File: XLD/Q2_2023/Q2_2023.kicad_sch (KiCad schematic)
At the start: 0 parts

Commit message: more updates
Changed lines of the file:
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@@
 (kicad_sch (version 20230121) (generator eeschema)
   (paper "A4")
-  (wire (pts (xy 263.525 36.195) (xy 263.525 37.465))
-    (stroke (width 0) (type default))
-  )
   (text "iqm5q\n" (at 91.44 36.195 0)
     (effects (font (size 5 5)) (justify left bottom))

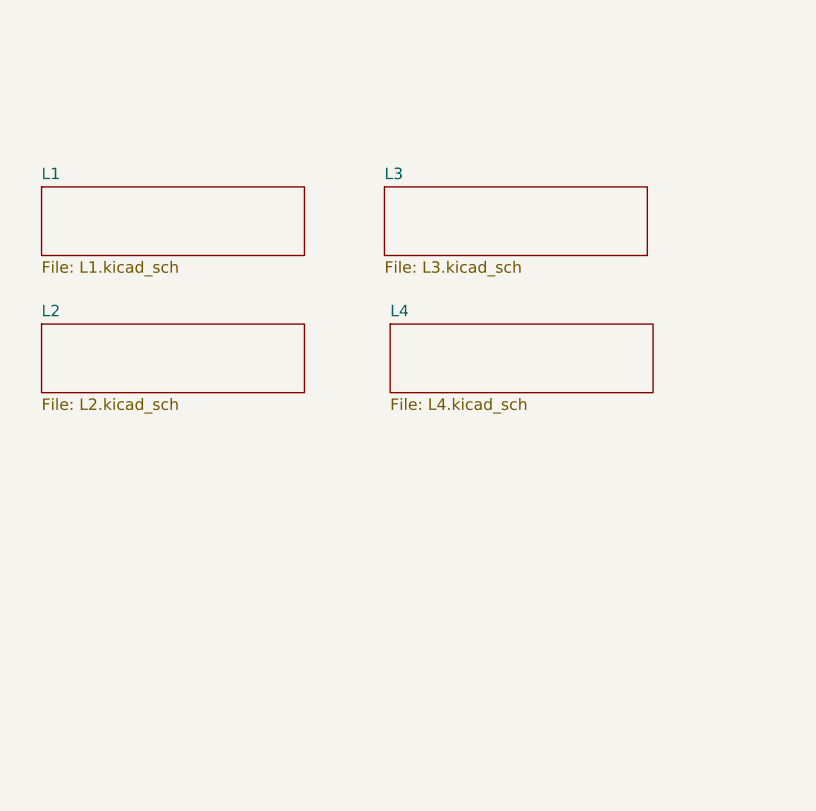
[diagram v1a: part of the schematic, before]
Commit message: update attenuators and pumplines
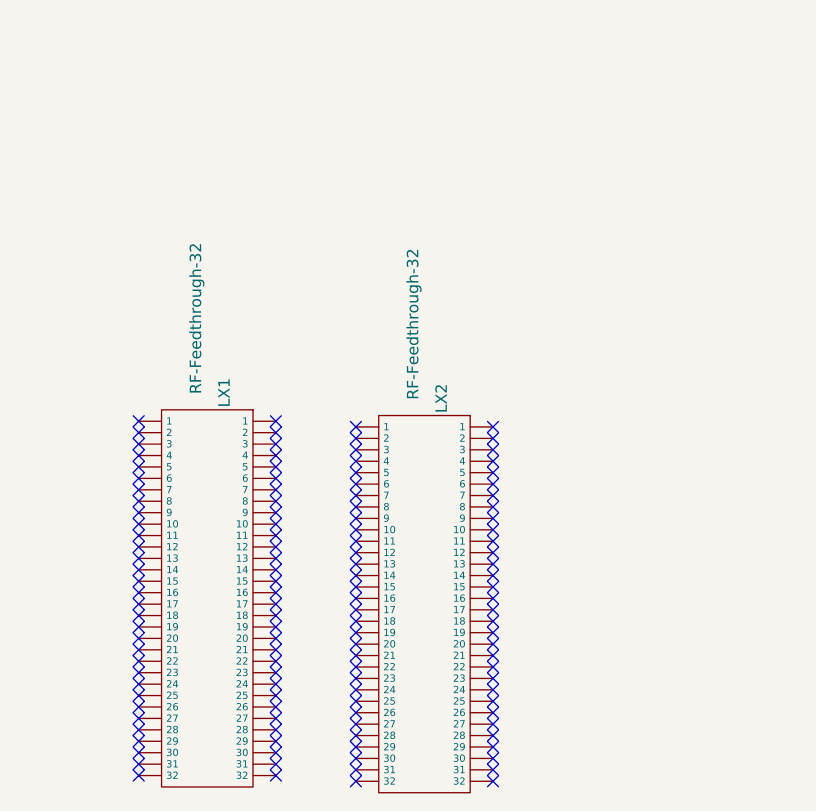
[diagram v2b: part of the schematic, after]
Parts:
- added LX1, LX2: RF-Feedthrough-32, symbol Quantum Computing:RF-Feedthrough-32
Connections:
- no-connect marks 0 -> 128
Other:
- removed sheet L1
- removed sheet L2
- removed sheet L3
- removed sheet L4

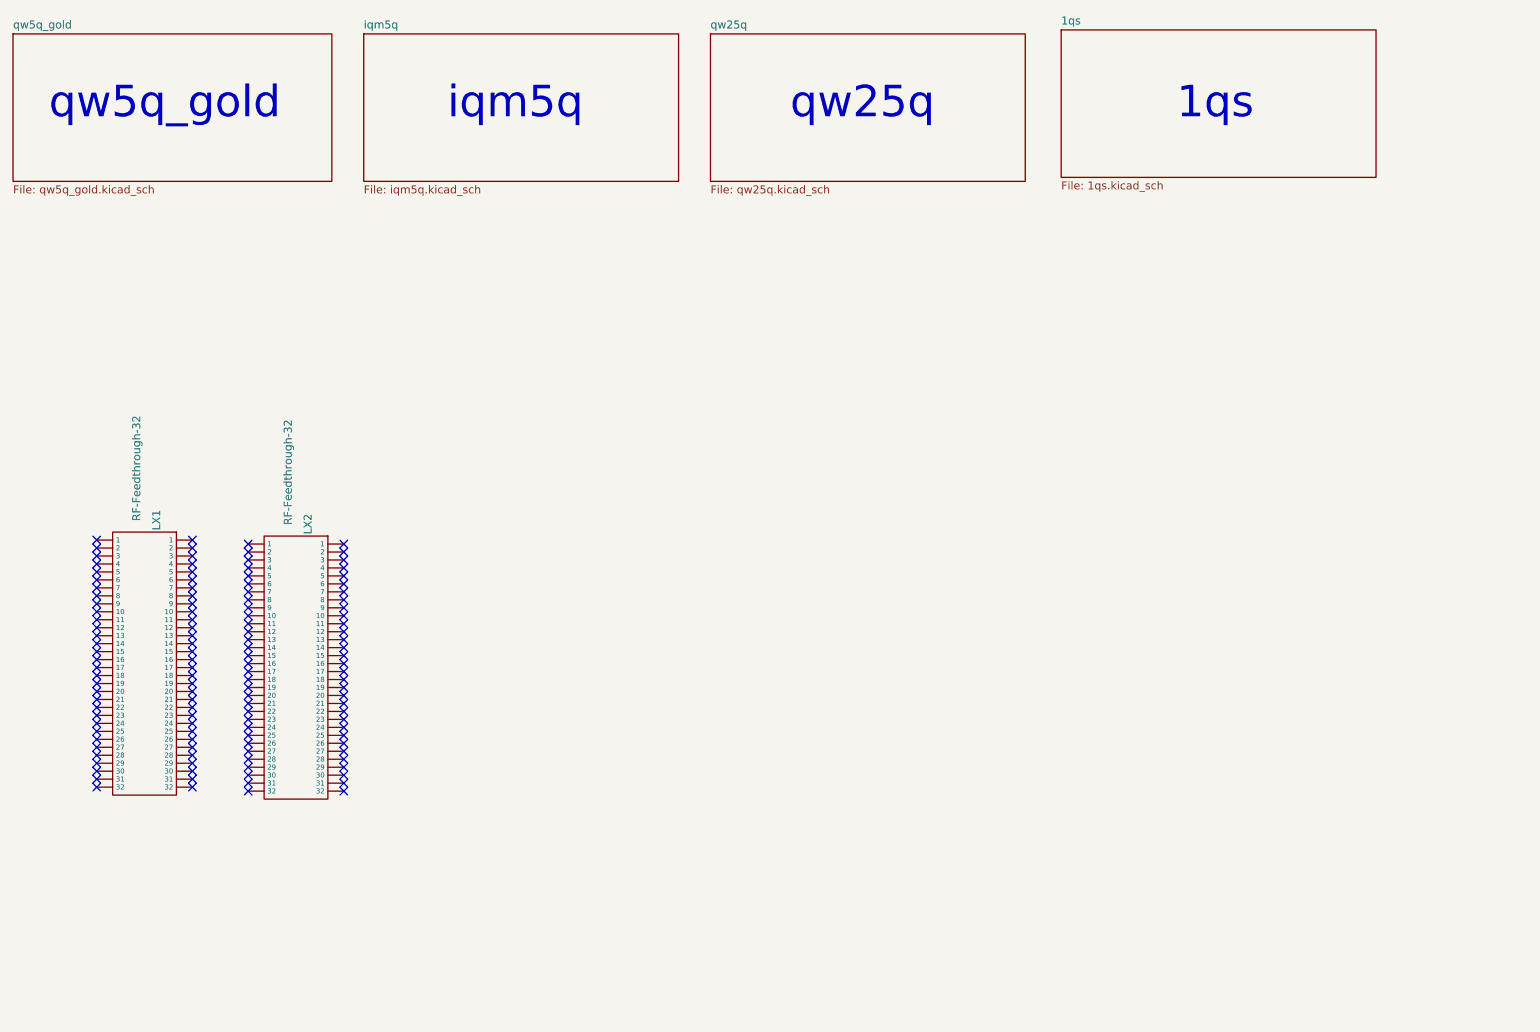
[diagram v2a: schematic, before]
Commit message: Improvements to library components, title, date
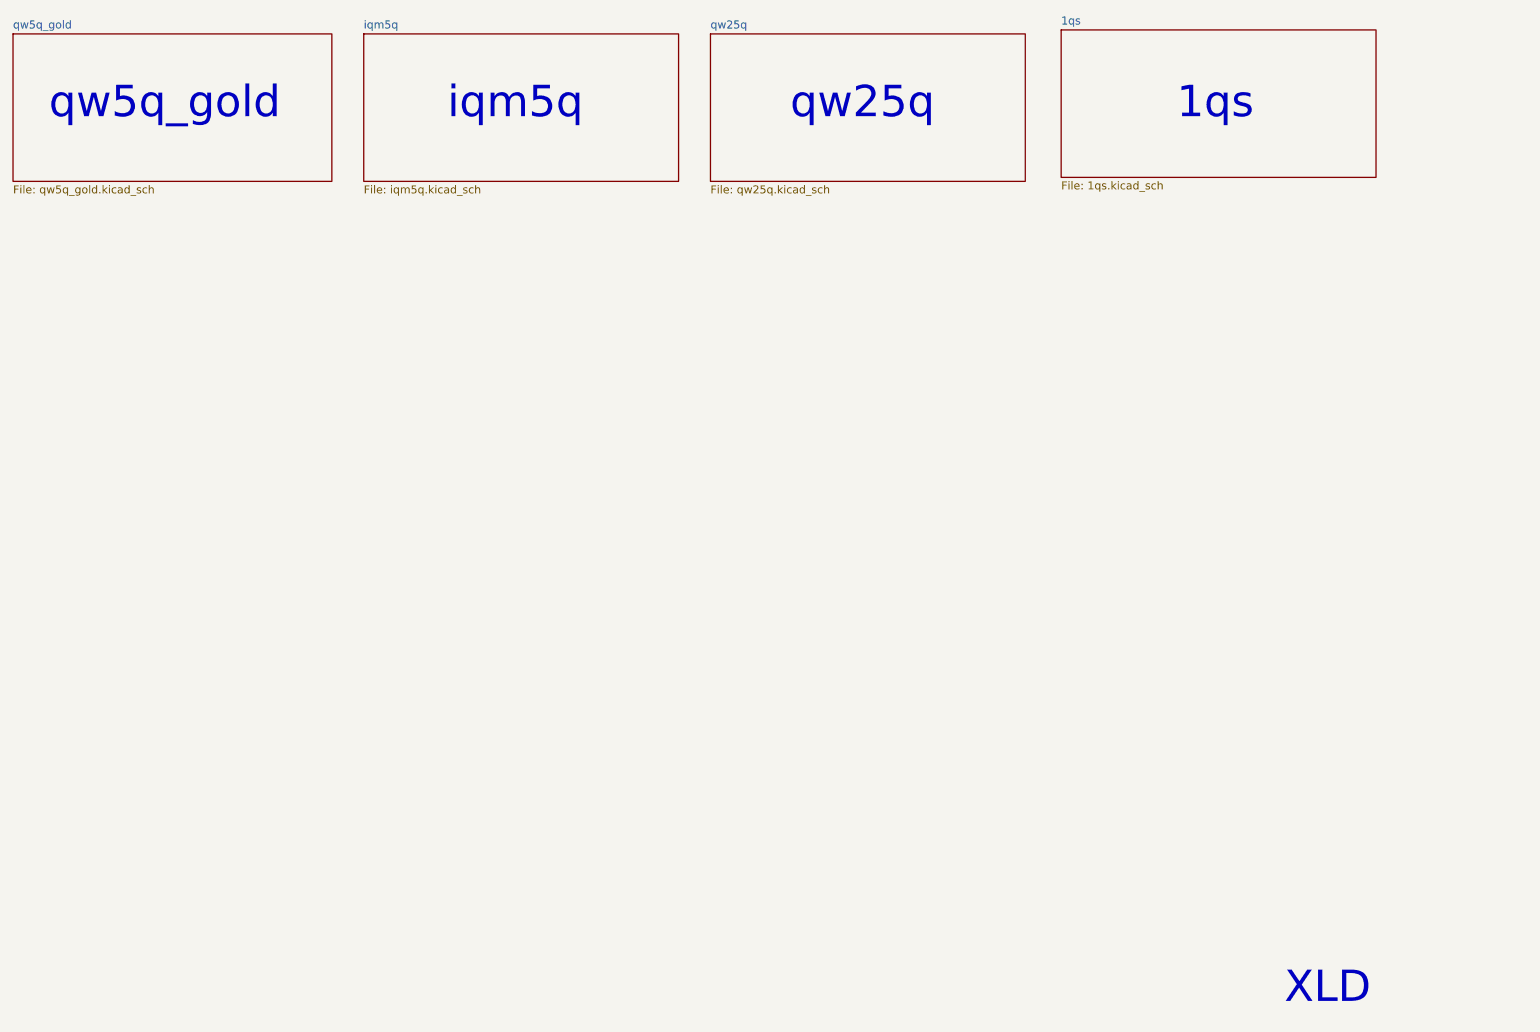
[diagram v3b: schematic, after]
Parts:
- removed LX1, LX2: RF-Feedthrough-32, symbol Quantum Computing:RF-Feedthrough-32
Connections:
- no-connect marks 128 -> 0
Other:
- note added: "XLD"
- company: (none) -> Technology Innovation Institute
- title: (none) -> XLD Setup Q2 2023
